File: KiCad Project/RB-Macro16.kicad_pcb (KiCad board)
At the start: 2 copper layers, 67 parts, among them J1 USB_C_Receptacle, J2 AVR-ISP-6, SW1 SW_PUSH, U1 ATMEGA32U4, X1 XTAL_GND

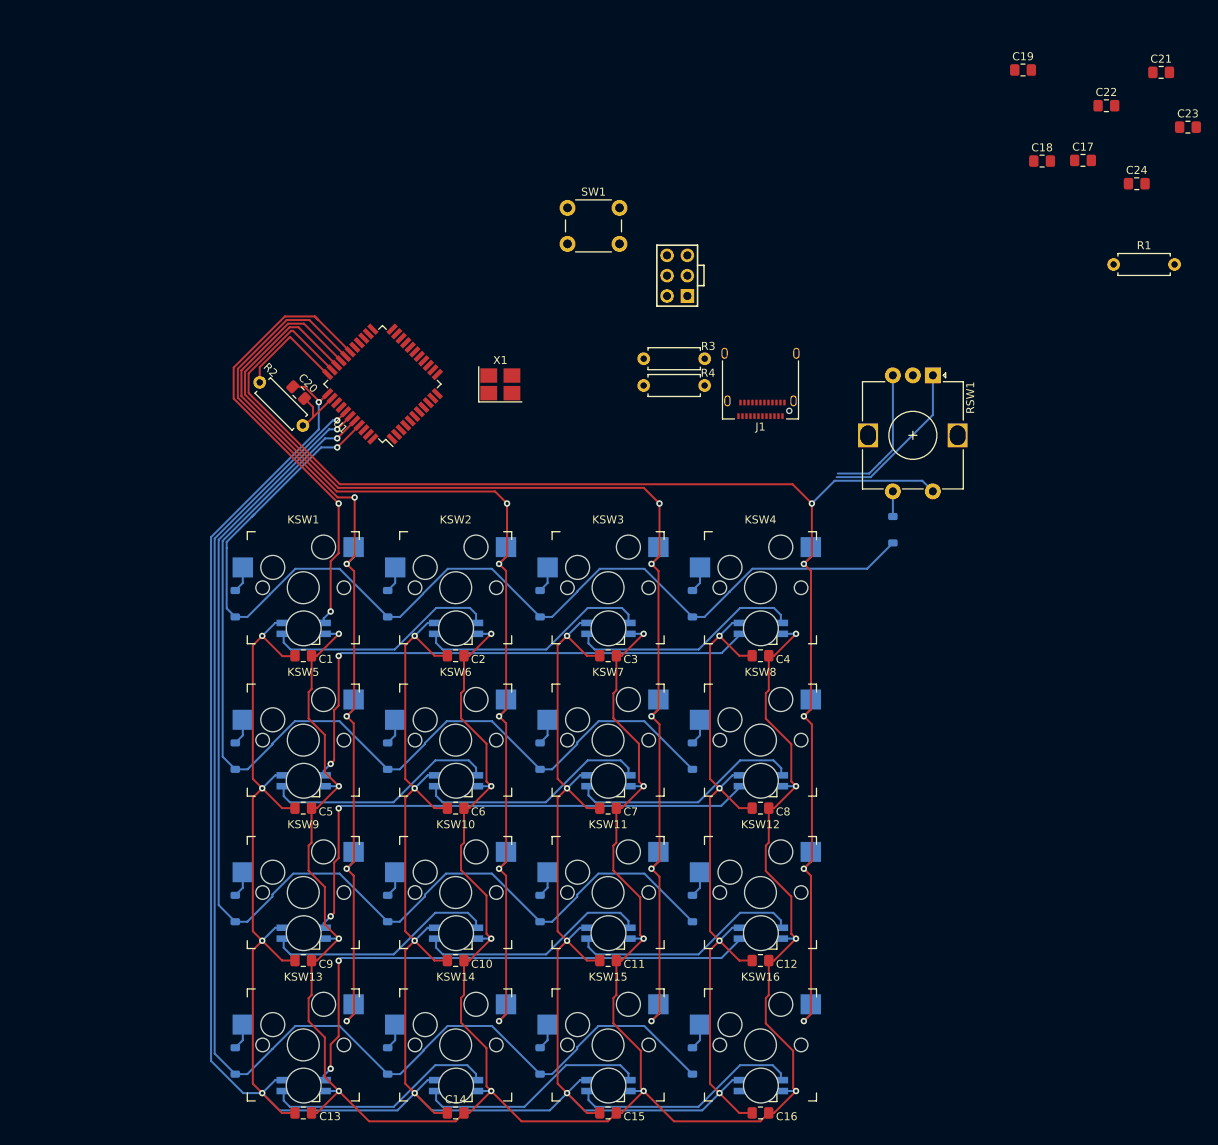
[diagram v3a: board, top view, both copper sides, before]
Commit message: Placed ATMEGA
Placed ATMEGA and XTAL and caps and routed traces to them
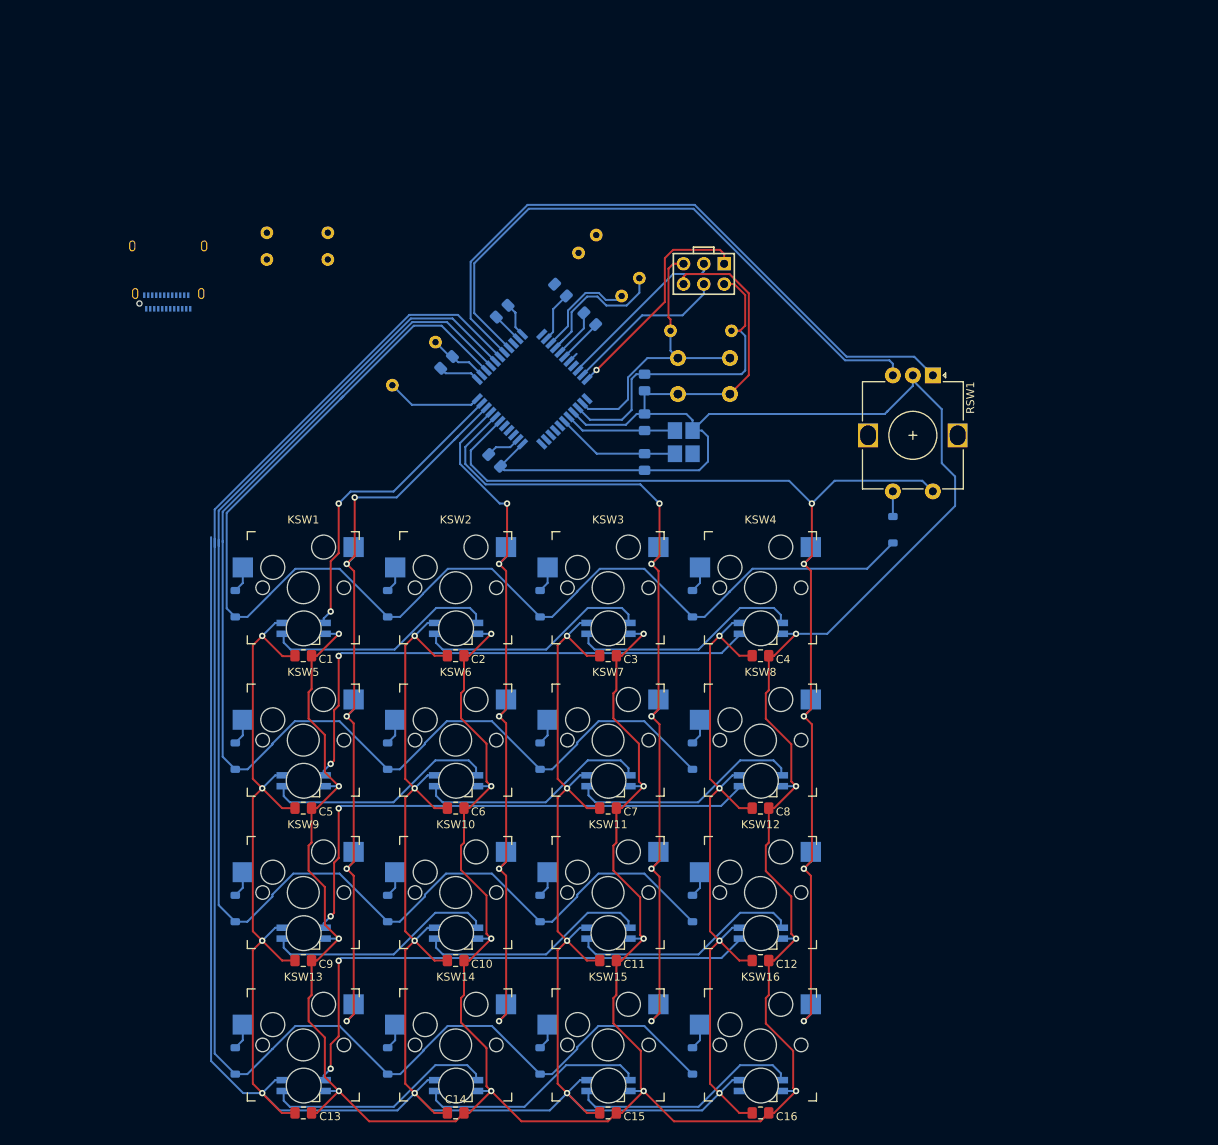
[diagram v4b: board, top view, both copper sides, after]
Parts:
- added R5: 22, Resistor_THT:R_Axial_DIN0207_L6.3mm_D2.5mm_P7.62mm_Horizontal, B.Cu at (108.8, 56.1)
- added R6: 22, Resistor_THT:R_Axial_DIN0207_L6.3mm_D2.5mm_P7.62mm_Horizontal, B.Cu at (111.0, 53.8)
- C1, C10, C11, C12, C13, C14, C15, C16, C2, C3, C4, C5, C6, C7, C8, C9: value C -> 0.1u
- C17, C18, C19, C20, C21, C22, C23, C24, J1, R1, R2, R3, R4, SW1, U1, X1: moved to B.Cu
- moved C23 96.2 mm to (98.3, 82.0), turned to -45 degrees
- moved C24 80.9 mm to (99.3, 63.3), turned to -135 degrees
- moved C21 79.9 mm to (106.6, 60.7), turned to 135 degrees
- moved J1 75.2 mm to (57.5, 58.0), turned to 0 degrees
- moved C22 67.3 mm to (117.1, 72.3), turned to -90 degrees
- moved C17 66.5 mm to (117.1, 82.2), turned to -90 degrees
- moved C19 62.5 mm to (110.2, 64.3), turned to 135 degrees
- moved C18 59.5 mm to (117.1, 77.2), turned to 90 degrees
- moved R3 56.9 mm to (69.9, 53.5), turned to 0 degrees
- moved R4 56.9 mm to (69.9, 56.9), turned to 0 degrees
- moved R1 48.5 mm to (127.9, 65.8), turned to 180 degrees
- moved SW1 27.1 mm to (121.2, 73.7)
- moved X1 24.0 mm to (122.0, 79.7), turned to 90 degrees
- moved C20 18.9 mm to (92.3, 69.7), turned to 45 degrees
- moved U1 18.7 mm to (103.0, 73.1), turned to -135 degrees
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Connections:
- C17 pad 1: Net-(U1-XTAL1) -> Net-(U1-XTAL2)
- C18 pad 1: Net-(U1-XTAL2) -> Net-(U1-XTAL1)
- J1 pad A6: Net-(U1-D+) -> Net-(J1-D+-PadA6)
- J1 pad A7: Net-(U1-D-) -> Net-(J1-D--PadA7)
- J1 pad B6: Net-(U1-D+) -> Net-(J1-D+-PadA6)
- J1 pad B7: Net-(U1-D-) -> Net-(J1-D--PadA7)
- U1 pad 28: /led0 -> /col3
- U1 pad 29: /col0 -> /col2
- U1 pad 31: /col2 -> /col0
- U1 pad 32: /col3 -> /led0
- U1 pad 36: /rotB -> /row0
- U1 pad 37: /rotA -> /row1
- U1 pad 38: /row3 -> /row2
- U1 pad 39: /row2 -> /row3
- U1 pad 40: /row1 -> /rotA
- U1 pad 41: /row0 -> /rotB
- X1 pad 1: Net-(U1-XTAL1) -> Net-(U1-XTAL2)
- X1 pad 2: Net-(U1-XTAL2) -> Net-(U1-XTAL1)
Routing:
- net GND: track 380.8 -> 557.7 mm
- net /rotA: track 20.2 -> 82.6 mm
- net /rotB: track 17.4 -> 77.0 mm
- net /col1: track 136.0 -> 93.1 mm
- net /col2: track 153.4 -> 111.1 mm
- net /col3: track 187.4 -> 145.7 mm
- net /RESET: track 0.00 -> 36.8 mm
- net VCC: track 540.3 -> 575.4 mm, vias 17 -> 16
- net /row3: track 163.3 -> 192.9 mm, vias 1 -> 0
- net /MISO: track 0.00 -> 28.5 mm, vias 0 -> 1
- net /row2: track 144.0 -> 172.3 mm, vias 1 -> 0
- net /row1: track 124.3 -> 151.0 mm, vias 1 -> 0
- net /row0: track 134.0 -> 159.5 mm, vias 1 -> 0
- net /SCK: track 0.00 -> 21.9 mm
- net /MOSI: track 0.00 -> 20.6 mm
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
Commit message: Minor Changes
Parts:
- moved R3 17.9 mm to (80.8, 67.8), turned to 45 degrees
- moved J1 14.6 mm to (71.5, 53.7)
- moved R4 12.3 mm to (78.5, 65.5), turned to 45 degrees
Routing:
- net GND: track 557.7 -> 565.6 mm
- net Net-(U1-D+): track 18.9 -> 17.5 mm
- net /row3: track 192.9 -> 191.8 mm
- net /row2: track 172.3 -> 171.5 mm
- net /row0: track 159.5 -> 159.0 mm
- net Net-(KSW12-DOUT): track 67.6 -> 67.1 mm
- net /col0: track 99.7 -> 99.2 mm
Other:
- board outline added: 96.9 x 116 mm

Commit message: Finished Traces
Completed all traces
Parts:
- added REF**: MountingHole_3.2mm_M3, MountingHole:MountingHole_3.2mm_M3, F.Cu at (48.0, 153.0)
- added REF**: MountingHole_3.2mm_M3, MountingHole:MountingHole_3.2mm_M3, F.Cu at (142.0, 153.0)
- added REF**: MountingHole_3.2mm_M3, MountingHole:MountingHole_3.2mm_M3, F.Cu at (142.0, 43.0)
- added REF**: MountingHole_3.2mm_M3, MountingHole:MountingHole_3.2mm_M3, F.Cu at (48.0, 43.0)
- moved R6 17.0 mm to (95.6, 46.7)
- moved J1 16.5 mm to (58.8, 43.2)
- moved C1 16.2 mm to (61.2, 97.0)
- moved C10 16.2 mm to (80.2, 135.1)
- moved C11 16.2 mm to (99.3, 135.1)
- moved C12 16.2 mm to (118.3, 135.1)
- moved C13 16.2 mm to (61.2, 154.2)
- moved C14 16.2 mm to (80.2, 154.2)
- moved C15 16.2 mm to (99.3, 154.2)
- moved C16 16.2 mm to (118.3, 154.2)
- moved C17 16.2 mm to (103.8, 72.8)
- moved C18 16.2 mm to (103.8, 67.8)
- moved C19 16.2 mm to (97.0, 54.9)
- moved C2 16.2 mm to (80.2, 97.0)
- moved C21 16.2 mm to (93.3, 51.3)
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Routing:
- net GND: track 565.6 -> 851.0 mm, vias 16 -> 21
- net VCC: track 575.3 -> 760.1 mm, vias 16 -> 26
- net Net-(J1-D--PadA7): track 0.00 -> 51.6 mm, vias 0 -> 2
- net Net-(J1-D+-PadA6): track 0.00 -> 43.2 mm, vias 0 -> 1
- net Net-(J1-CC1): track 0.00 -> 17.1 mm
- net Net-(J1-CC2): track 0.00 -> 15.0 mm, vias 0 -> 1
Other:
- board size 96.9 x 116 mm -> 102 x 118 mm

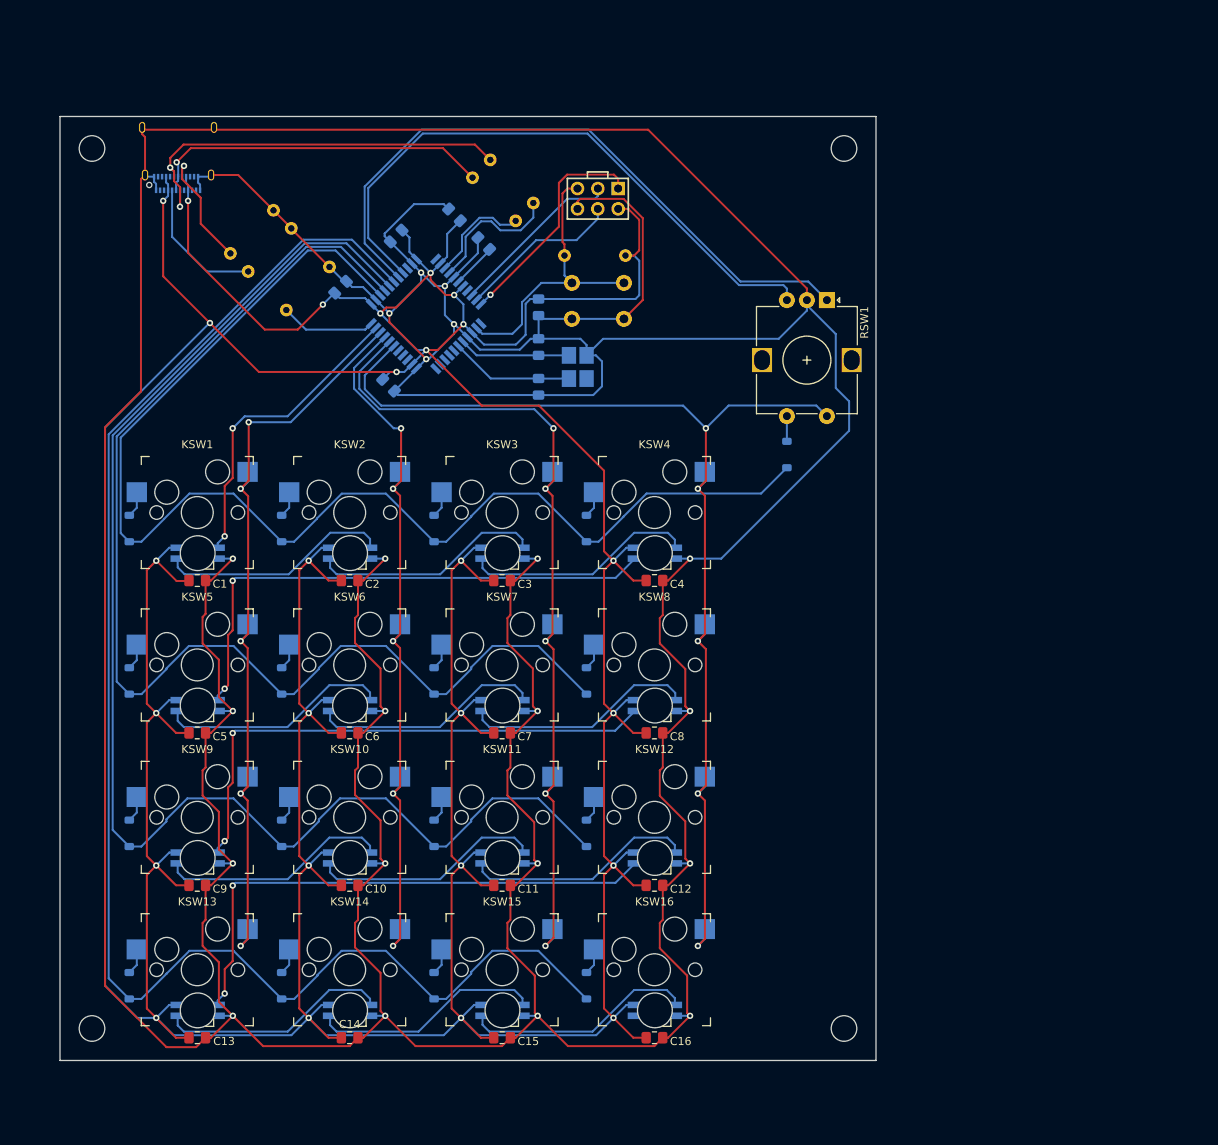
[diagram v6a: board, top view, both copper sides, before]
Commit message: Added Graphics and Finalized
Added a graphic and finalized the design including integrity checks. Generated Gerber files.
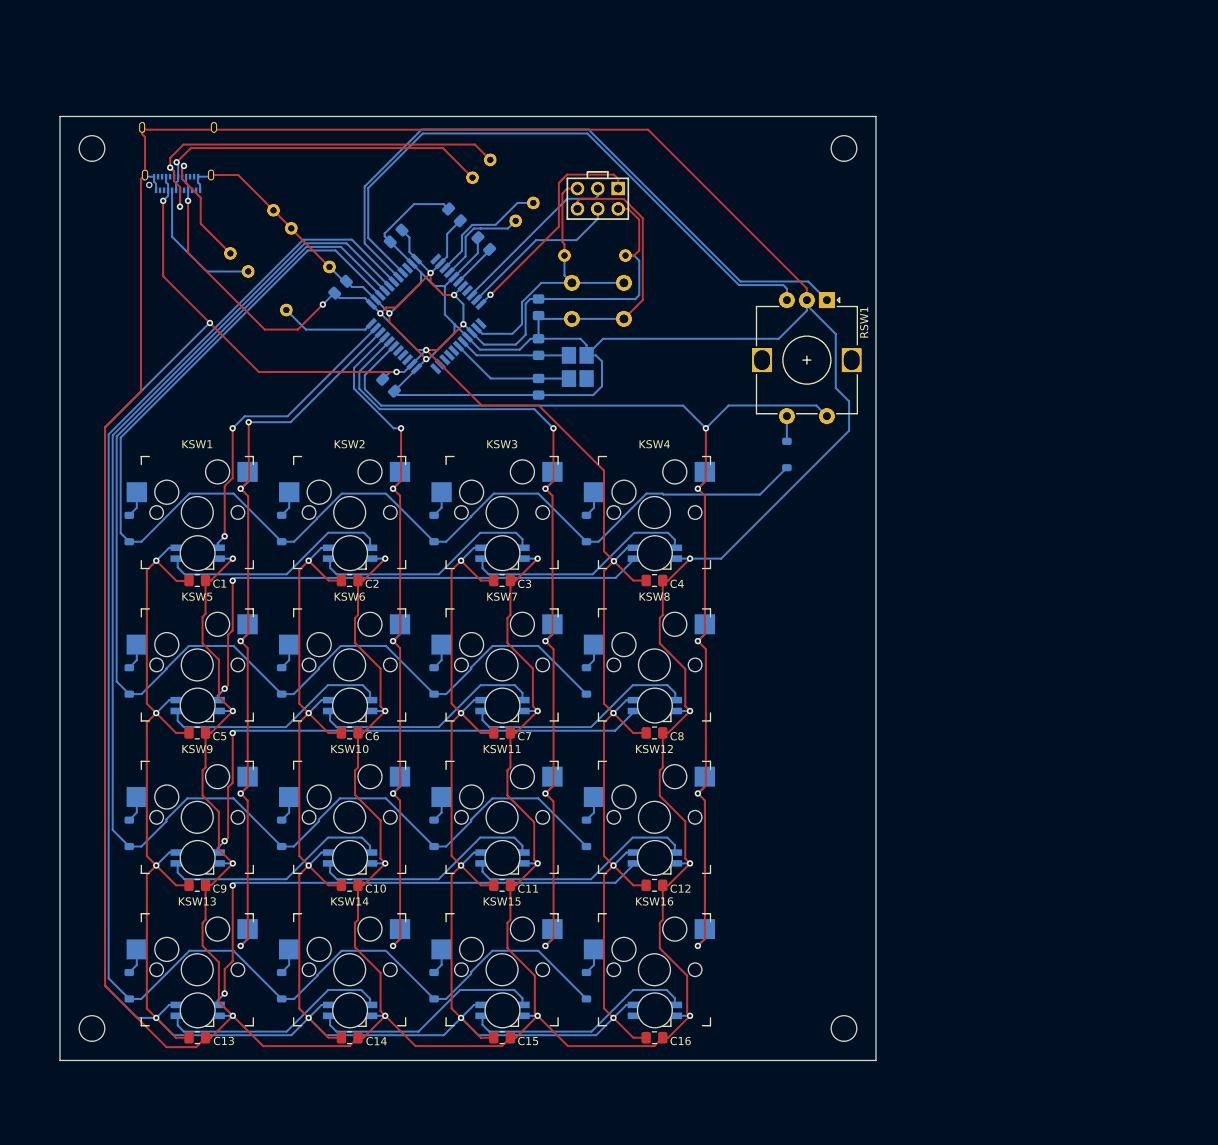
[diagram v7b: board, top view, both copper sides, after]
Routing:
- net Net-(U1-D+): track 17.5 -> 12.4 mm
- net Net-(U1-D-): track 13.2 -> 15.6 mm
- net GND: track 851.0 -> 850.7 mm, vias 21 -> 18
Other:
- board text added: "RB-Macro16"
